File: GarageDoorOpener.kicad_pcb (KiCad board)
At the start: 2 copper layers, 41 x 57 mm, 30 parts, among them J1 USB_B_Mini, J2 Door Sensor, J3 FTDI, J4 Conn_01x16, J6 Door Switch, Q1 Q_NPN_BEC, SW1 RESET, SW2 FLASH, U1 AMS1117-3.3, U2 ESP32-C3-WROOM-02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

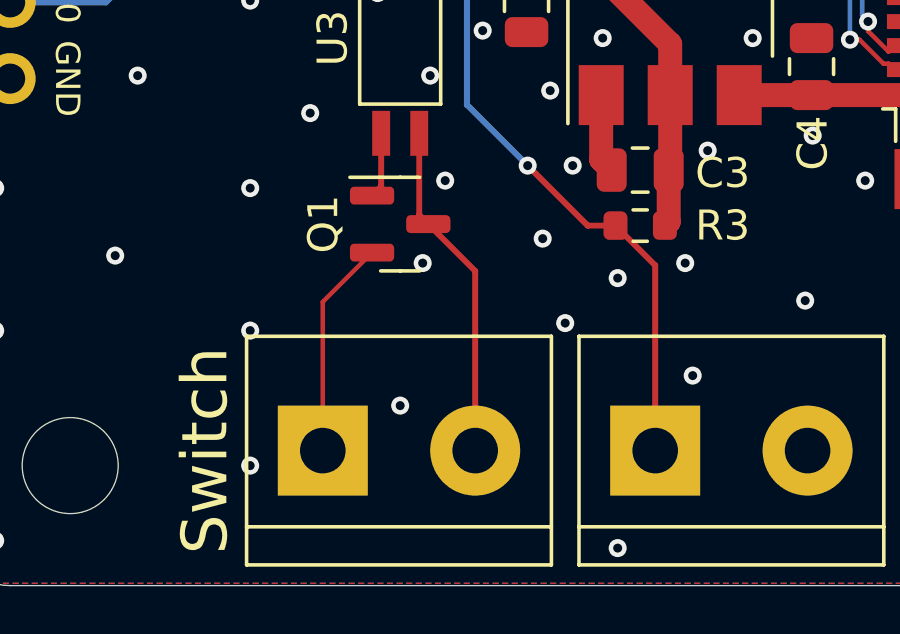
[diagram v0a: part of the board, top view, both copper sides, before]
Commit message: Board rev 1.1, add switch capacitor
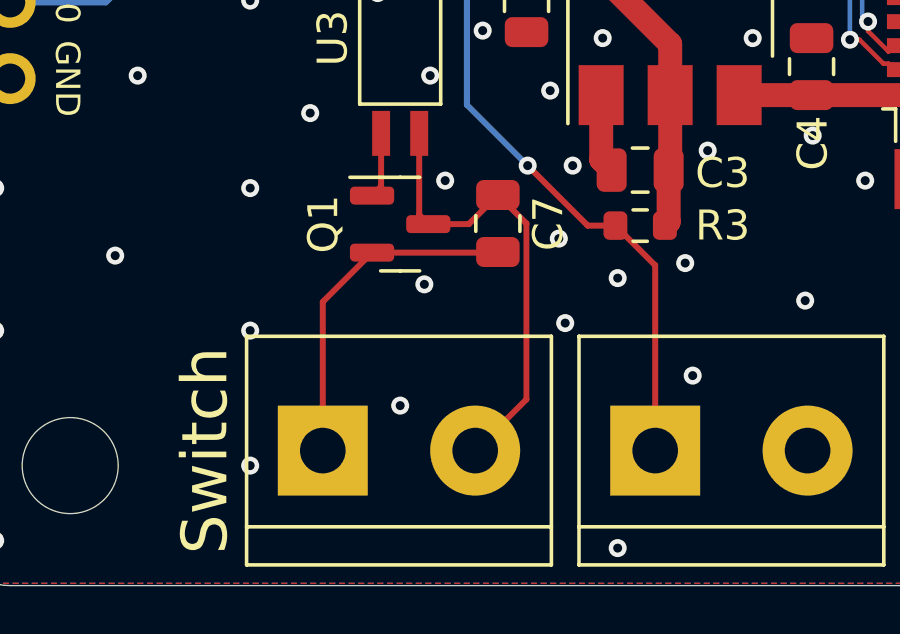
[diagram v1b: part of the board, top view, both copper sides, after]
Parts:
- added C7: 0.1u, Capacitor_SMD:C_0805_2012Metric, F.Cu at (108.3, 94.9)
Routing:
- net DOOR_SWITCH-: track 7.28 -> 11.5 mm
- net DOOR_SWITCH+: track 11.3 -> 15.5 mm
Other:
- board text added: "Garage Door Opener v1.1"
- board text removed: "Garage Door Opener v1.0"
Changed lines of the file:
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@@
+    )
+  )
+  (footprint "Capacitor_SMD:C_0805_2012Metric" (layer "F.Cu")
+    (at 108.256 94.93 -90)
+    (descr "Capacitor SMD 0805 (2012 Metric), square (rectangular) end terminal, IPC_7351 nominal, (Body size source: IPC-SM-782 page 76, https://www.pcb-3d.com/wordpress/wp-content/uploads/ipc-sm-782a_amendment_1_and_2.pdf, https://docs.google.com/spreadsheets/d/1BsfQQcO9C6DZCsRaXUlFlo91Tg2WpOkGARC1WS5S8t0/edit?usp=sharing), generated with kicad-footprint-generator")
+    (tags "capacitor")
+    (property "Sheetfile" "GarageDoorOpener.kicad_sch")
+    (property "Sheetname" "")
+    (attr smd)
+    (fp_text reference "C7" (at 0 -1.68 90) (layer "F.SilkS")
+      (effects (font (size 1 1) (thickness 0.15)))
+    )
+    (fp_text value "0.1u" (at 0 1.68 90) (layer "F.Fab")
+      (effects (font (size 1 1) (thickness 0.15)))
+    )
+    (fp_text user "${REFERENCE}" (at 0 0 90) (layer "F.Fab")
+      (effects (font (size 0.5 0.5) (thickness 0.08)))
+    )
+    (fp_line (start -0.261252 -0.735) (end 0.261252 -0.735) (layer "F.SilkS") (width 0.12))
+    (fp_line (start -0.261252 0.735) (end 0.261252 0.735) (layer "F.SilkS") (width 0.12))
+    (fp_line (start 1.7 -0.98) (end 1.7 0.98) (layer "F.CrtYd") (width 0.05))
+    (fp_line (start -1.7 -0.98) (end 1.7 -0.98) (layer "F.CrtYd") (width 0.05))
+    (fp_line (start -1.7 0.98) (end -1.7 -0.98) (layer "F.CrtYd") (width 0.05))
+    (fp_line (start 1.7 0.98) (end -1.7 0.98) (layer "F.CrtYd") (width 0.05))
+    (fp_line (start 1 0.625) (end -1 0.625) (layer "F.Fab") (width 0.1))
+    (fp_line (start -1 -0.625) (end 1 -0.625) (layer "F.Fab") (width 0.1))
+    (fp_line (start 1 -0.625) (end 1 0.625) (layer "F.Fab") (width 0.1))
+    (fp_line (start -1 0.625) (end -1 -0.625) (layer "F.Fab") (width 0.1))
+    (pad "1" smd roundrect (at -0.95 0 270) (size 1 1.45) (layers "F.Cu" "F.Paste" "F.Mask") (roundrect_rratio 0.25)
+      (net 25 "DOOR_SWITCH+") (pintype "passive"))
+    (pad "2" smd roundrect (at 0.95 0 270) (size 1 1.45) (layers "F.Cu" "F.Paste" "F.Mask") (roundrect_rratio 0.25)
+      (net 24 "DOOR_SWITCH-") (pintype "passive"))
+    (model "${KICAD6_3DMODEL_DIR}/Capacitor_SMD.3dshapes/C_0805_2012Metric.wrl"
+      (offset (xyz 0 0 0))
+      (scale (xyz 1 1 1))
+      (rotate (xyz 0 0 0))
     )
   )
@@
     (property "Sheetfile" "GarageDoorOpener.kicad_sch")
     (property "Sheetname" "")
-    (attr through_hole exclude_from_pos_files exclude_from_bom)
+    (attr through_hole exclude_from_pos_files)
     (fp_text reference "J6" (at 2.54 -5.08) (layer "F.SilkS") hide
       (effects (font (size 1 1) (thickness 0.15)))
@@
     (property "Sheetfile" "GarageDoorOpener.kicad_sch")
     (property "Sheetname" "")
-    (attr through_hole exclude_from_pos_files exclude_from_bom)
+    (attr through_hole exclude_from_pos_files)
     (fp_text reference "J2" (at 2.54 -5.08) (layer "F.SilkS") hide
       (effects (font (size 1 1) (thickness 0.15)))
@@
     (property "Sheetfile" "GarageDoorOpener.kicad_sch")
     (property "Sheetname" "")
-    (attr exclude_from_pos_files exclude_from_bom)
+    (attr exclude_from_pos_files)
     (fp_text reference "H3" (at 0 -4.2) (layer "F.SilkS") hide
       (effects (font (size 1 1) (thickness 0.15)))
@@
     (property "Sheetfile" "GarageDoorOpener.kicad_sch")
     (property "Sheetname" "")
-    (attr exclude_from_pos_files exclude_from_bom)
+    (attr exclude_from_pos_files)
     (fp_text reference "H2" (at 0 -4.2) (layer "F.SilkS") hide
       (effects (font (size 1 1) (thickness 0.15)))
@@
     (property "Sheetfile" "GarageDoorOpener.kicad_sch")
     (property "Sheetname" "")
-    (attr through_hole exclude_from_pos_files exclude_from_bom)
+    (attr through_hole exclude_from_pos_files)
     (fp_text reference "J3" (at 0 -2.33) (layer "F.SilkS") hide
       (effects (font (size 1 1) (thickness 0.15)))
@@
     (property "Sheetfile" "GarageDoorOpener.kicad_sch")
     (property "Sheetname" "")
-    (attr exclude_from_pos_files exclude_from_bom)
+    (attr exclude_from_pos_files)
     (fp_text reference "H1" (at 0 -4.2) (layer "F.SilkS") hide
       (effects (font (size 1 1) (thickness 0.15)))
@@
     (property "Sheetfile" "GarageDoorOpener.kicad_sch")
     (property "Sheetname" "")
-    (attr through_hole exclude_from_pos_files exclude_from_bom)
+    (attr through_hole exclude_from_pos_files)
     (fp_text reference "J4" (at 0 -2.33) (layer "F.SilkS") hide
       (effects (font (size 1 1) (thickness 0.15)))
@@
     (effects (font (size 0.8128 0.8128) (thickness 0.1524)) (justify mirror))
   )
-  (gr_text "Garage Door Opener v1.0" (at 111 52.254) (layer "B.SilkS")
+  (gr_text "Garage Door Opener v1.1" (at 111 52.254) (layer "B.SilkS")
     (effects (font (size 1 1) (thickness 0.1524)) (justify mirror))
   )
@@
     (pts (xy 90 50) (xy 90 78.5))
     (height 3.174999)
-    (gr_text "28.5000 mm" (at 85.675001 64.25 90) (layer "F.Fab")
+    (gr_text "1.1220 in" (at 85.675001 64.25 90) (layer "F.Fab")
       (effects (font (size 1 1) (thickness 0.15)))
     )
@@
     (pts (xy 90 50) (xy 90 107))
     (height 6.35)
-    (gr_text "57.0000 mm" (at 82.5 78.5 90) (layer "F.Fab")
+    (gr_text "2.2441 in" (at 82.5 78.5 90) (layer "F.Fab")
       (effects (font (size 1 1) (thickness 0.15)))
     )
@@
     (pts (xy 90 50) (xy 131 50))
     (height -6.5)
-    (gr_text "41.0000 mm" (at 110.5 42.35) (layer "F.Fab")
+    (gr_text "1.6142 in" (at 110.5 42.35) (layer "F.Fab")
       (effects (font (size 1 1) (thickness 0.15)))
     )
@@
   (via (at 110.5 98.25) (size 0.6) (drill 0.3) (layers "F.Cu" "B.Cu") (free) (net 2))
   (via (at 113.5 56.25) (size 0.6) (drill 0.3) (layers "F.Cu" "B.Cu") (free) (net 2))
-  (via (at 109.75 95.434) (size 0.6) (drill 0.3) (layers "F.Cu" "B.Cu") (free) (net 2))
+  (via (at 110.288 95.434) (size 0.6) (drill 0.3) (layers "F.Cu" "B.Cu") (free) (net 2))
   (via (at 93.75 86.25) (size 0.6) (drill 0.3) (layers "F.Cu" "B.Cu") (free) (net 2))
   (via (at 113 69) (size 0.6) (drill 0.3) (layers "F.Cu" "B.Cu") (free) (net 2))
@@
   (via (at 97.25 58.25) (size 0.6) (drill 0.3) (layers "F.Cu" "B.Cu") (free) (net 2))
   (via (at 100.25 55) (size 0.6) (drill 0.3) (layers "F.Cu" "B.Cu") (free) (net 2))
-  (via (at 105.75 96.25) (size 0.6) (drill 0.3) (layers "F.Cu" "B.Cu") (free) (net 2))
+  (via (at 105.805416 96.958) (size 0.6) (drill 0.3) (layers "F.Cu" "B.Cu") (free) (net 2))
   (via (at 127.75 73.5) (size 0.6) (drill 0.3) (layers "F.Cu" "B.Cu") (free) (net 2))
   (via (at 124.5 75) (size 0.6) (drill 0.3) (layers "F.Cu" "B.Cu") (free) (net 2))
@@
   (segment (start 105.825 83.5) (end 105.635 83.69) (width 0.2) (layer "F.Cu") (net 23))
   (segment (start 105.635 83.69) (end 105.635 85.575) (width 0.2) (layer "F.Cu") (net 23))
-  (segment (start 104.0625 95.9) (end 102.42 97.5425) (width 0.1524) (layer "F.Cu") (net 24))
-  (segment (start 102.42 97.5425) (end 102.42 102.5) (width 0.1524) (layer "F.Cu") (net 24))
-  (segment (start 105.9375 94.95) (end 107.5 96.5125) (width 0.2) (layer "F.Cu") (net 25))
+  (segment (start 104.0625 95.9) (end 102.42 97.5425) (width 0.2) (layer "F.Cu") (net 24))
+  (segment (start 102.42 97.5425) (end 102.42 102.5) (width 0.2) (layer "F.Cu") (net 24))
+  (segment (start 104.0625 95.9) (end 108.236 95.9) (width 0.2) (layer "F.Cu") (net 24))
+  (segment (start 108.236 95.9) (end 108.256 95.88) (width 0.2) (layer "F.Cu") (net 24))
+  (segment (start 107.286 94.95) (end 108.256 93.98) (width 0.2) (layer "F.Cu") (net 25))
+  (segment (start 108.256 93.98) (end 109.208 94.932) (width 0.2) (layer "F.Cu") (net 25))
   (segment (start 105.635 91.925) (end 105.635 94.6475) (width 0.2) (layer "F.Cu") (net 25))
-  (segment (start 107.5 96.5125) (end 107.5 102.5) (width 0.2) (layer "F.Cu") (net 25))
+  (segment (start 109.208 94.932) (end 109.208 100.792) (width 0.2) (layer "F.Cu") (net 25))
+  (segment (start 105.9375 94.95) (end 107.286 94.95) (width 0.2) (layer "F.Cu") (net 25))
+  (segment (start 109.208 100.792) (end 107.5 102.5) (width 0.2) (layer "F.Cu") (net 25))
   (segment (start 105.635 94.6475) (end 105.9375 94.95) (width 0.2) (layer "F.Cu") (net 25))
   (segment (start 119.25 57.2) (end 119.55 57.2) (width 0.1524) (layer "F.Cu") (net 26))
